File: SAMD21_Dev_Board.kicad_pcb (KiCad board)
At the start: 2 copper layers, 55.4 x 87.4 mm, 88 parts, among them J1 SWD, J10 JST_SH_SM06B-SRSS-TB_1x06-1MP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, J11 JST_SH_SM06B-SRSS-TB_1x06-1MP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, J12 JST_SH_SM06B-SRSS-TB_1x06-1MP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, J13 JST_SH_SM06B-SRSS-TB_1x06-1MP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, J14 JST_SH_SM06B-SRSS-TB_1x06-1MP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, J15 JST_SH_SM06B-SRSS-TB_1x06-1MP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, J16 JST_SH_SM06B-SRSS-TB_1x06-1MP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, J17 Status LED, J2 USB_C_Receptacle_USB2.0_16P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

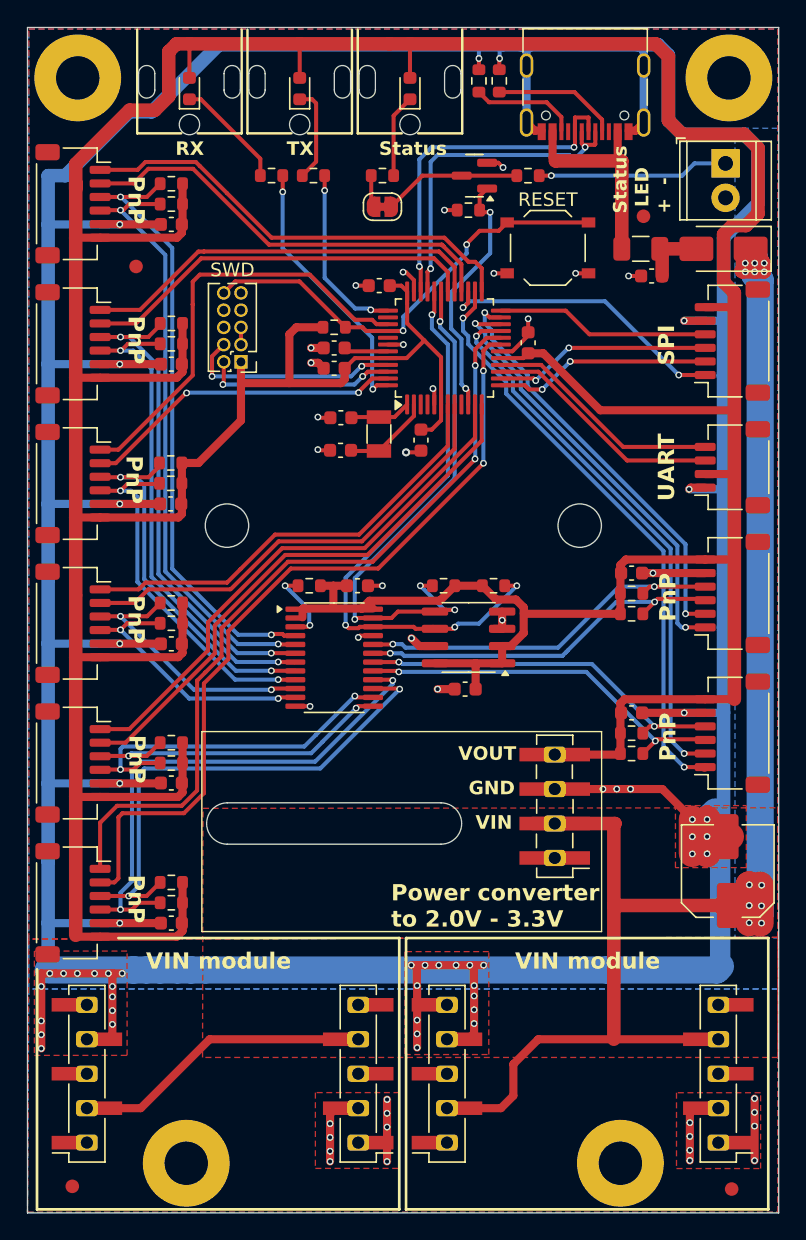
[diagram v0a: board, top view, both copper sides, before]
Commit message: Back to cables with GND pin1, VCC pin2
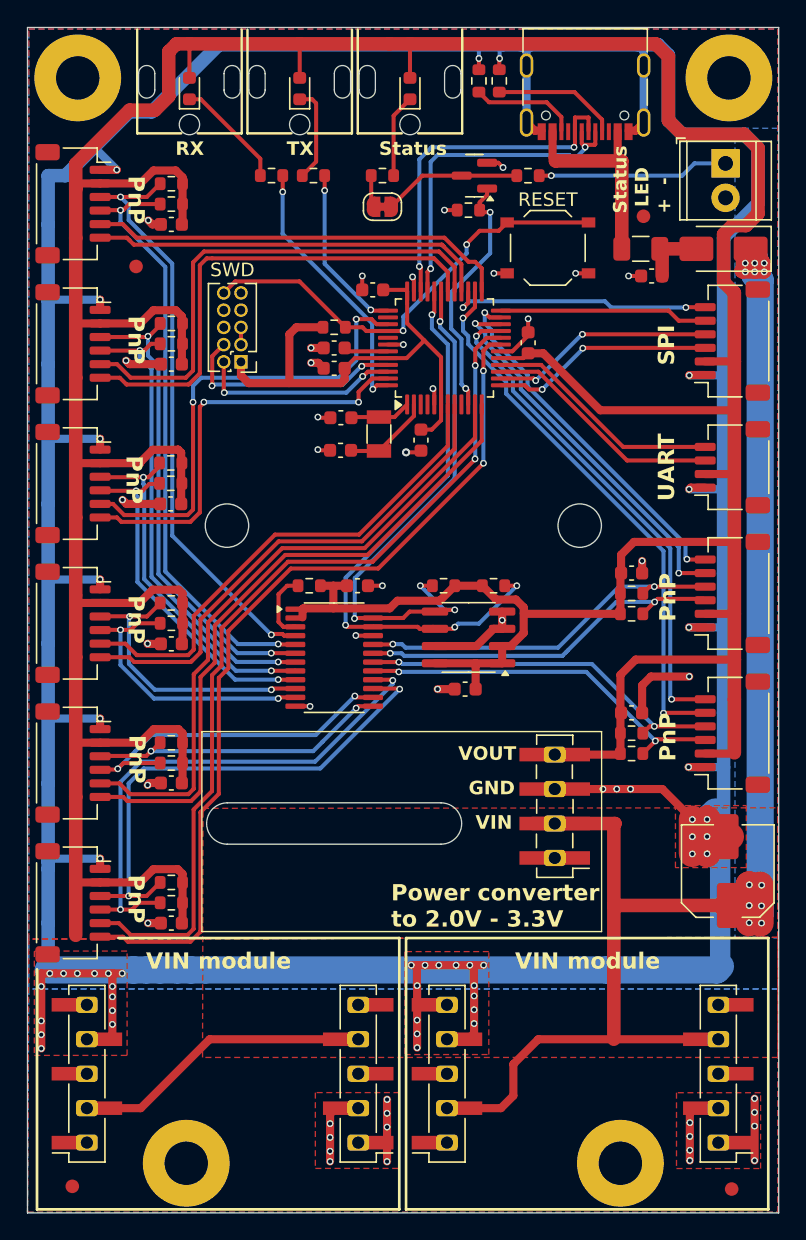
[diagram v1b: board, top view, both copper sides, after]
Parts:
- moved C16 0.57 mm to (107.7, 69.1)
- turned C5 to 180 degrees
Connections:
- C5 pad 1: GND -> VCC
- C5 pad 2: VCC -> GND
- J10 pad 1: D13 -> GND
- J10 pad 2: D22 -> VCC
- J10 pad 5: GND -> D13
- J10 pad 6: VCC -> D22
- J11 pad 1: D24 -> GND
- J11 pad 2: D23 -> VCC
- J11 pad 5: GND -> D24
- J11 pad 6: VCC -> D23
- J12 pad 1: D8 -> GND
- J12 pad 2: D9 -> VCC
- J12 pad 5: GND -> D8
- J12 pad 6: VCC -> D9
- J13 pad 1: D11 -> GND
- J13 pad 2: D12 -> VCC
- J13 pad 5: GND -> D11
- J13 pad 6: VCC -> D12
- J14 pad 1: D6 -> GND
- J14 pad 2: D7 -> VCC
- J14 pad 5: GND -> D6
- J14 pad 6: VCC -> D7
- J15 pad 1: D26 -> GND
- J15 pad 2: A5 -> VCC
- J15 pad 5: GND -> D26
- J15 pad 6: VCC -> A5
- J16 pad 1: A1 -> GND
- J16 pad 2: A2 -> VCC
- J16 pad 5: GND -> A1
- J16 pad 6: VCC -> A2
- J8 pad 1: D10/SPI_SS -> GND
- J8 pad 2: SPI_MOSI -> VCC
- J8 pad 3: SPI_MISO -> SPI_MOSI
- J8 pad 4: SPI_SCK -> SPI_MISO
- J8 pad 5: GND -> SPI_SCK
- J8 pad 6: VCC -> D10/SPI_SS
- J9 pad 1: D38 -> GND
- J9 pad 2: D2 -> VCC
- J9 pad 5: GND -> D38
- J9 pad 6: VCC -> D2
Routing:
- net GND: track 447.4 -> 427.9 mm, vias 86 -> 93
- net D8: track 40.2 -> 47.9 mm
- net D9: track 41.2 -> 48.5 mm
- net D6: track 30.2 -> 37.3 mm
- net A5: track 23.9 -> 30.8 mm
- net D7: track 29.5 -> 36.2 mm
- net D24: track 58.4 -> 64.7 mm
- net VCC: track 381.0 -> 387.0 mm
- net D23: track 59.4 -> 64.6 mm
- net D2: track 31.1 -> 27.0 mm
- net D38: track 32.4 -> 28.5 mm
- net A1: track 33.1 -> 36.9 mm
- net D22: track 40.6 -> 37.2 mm
- net A2: track 34.0 -> 37.5 mm
- net D13: track 43.8 -> 40.7 mm
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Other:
- board text added: "GND VCC SDA SCL INT1 INT2"
- board text added: "SS SCK MISO MOSI VCC GND"
- board text removed: "INT2 INT1 SDA SCL GND VCC"
- board text removed: "VCC GND SCK MISO MOSI SS"

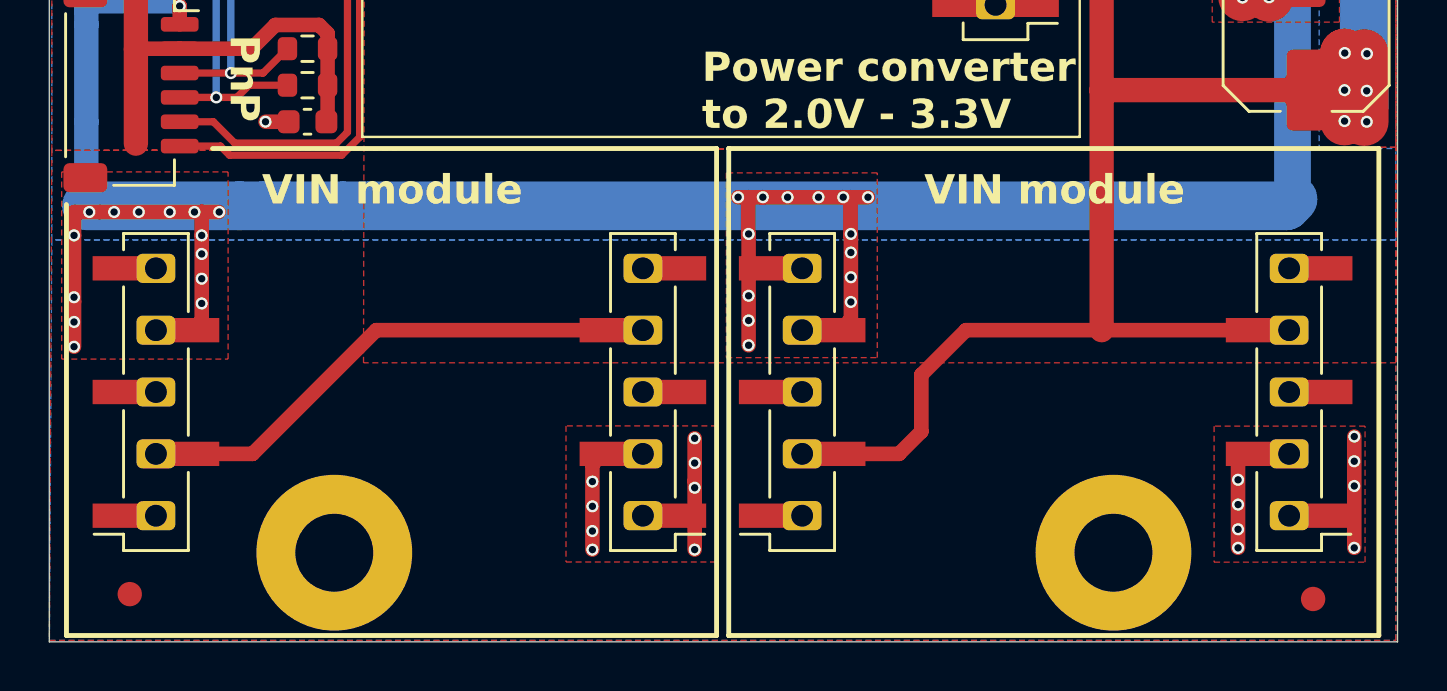
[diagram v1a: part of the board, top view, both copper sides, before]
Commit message: Moved the power modules location to have 1mm more spacing between them
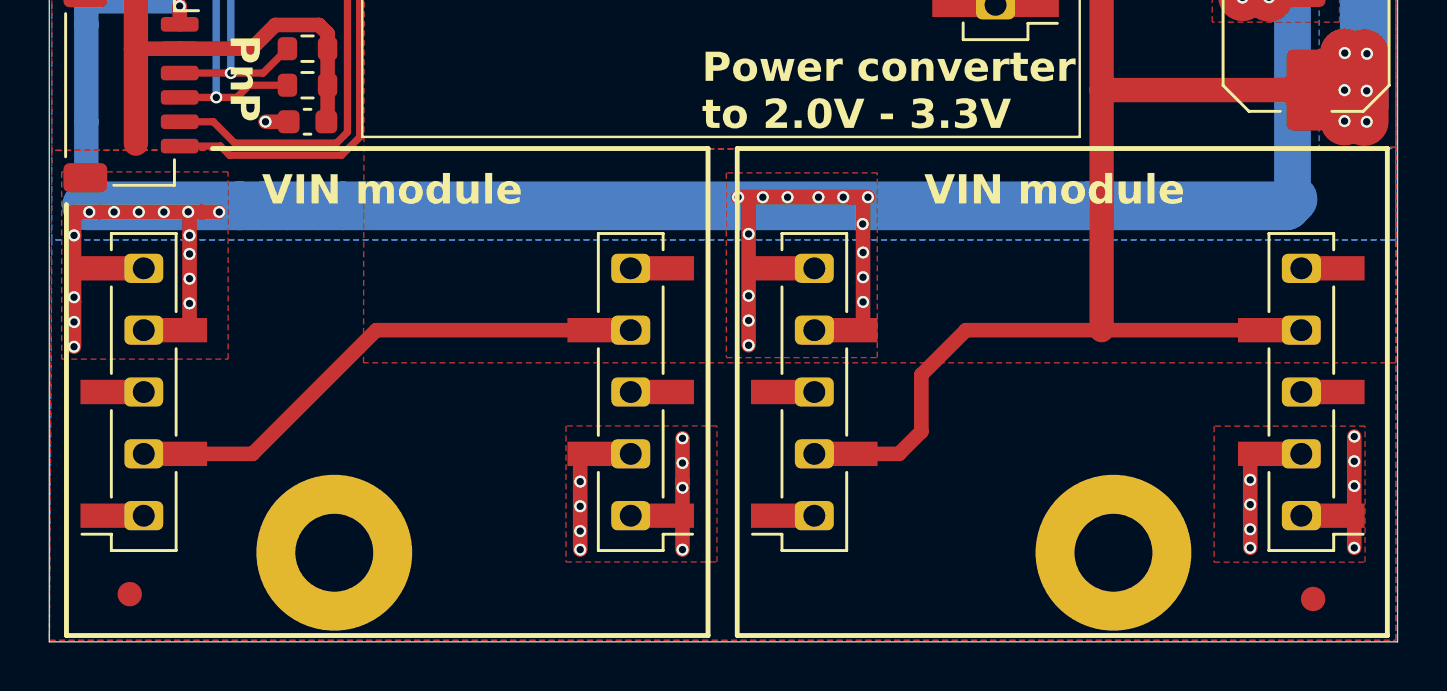
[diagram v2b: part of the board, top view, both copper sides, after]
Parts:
- moved J20 0.50 mm to (86.2, 126.9)
- moved J4 0.50 mm to (106.2, 126.9)
- moved J5 0.50 mm to (113.7, 126.9)
- moved J6 0.50 mm to (133.7, 126.9)
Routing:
- net GND: track 427.9 -> 425.3 mm

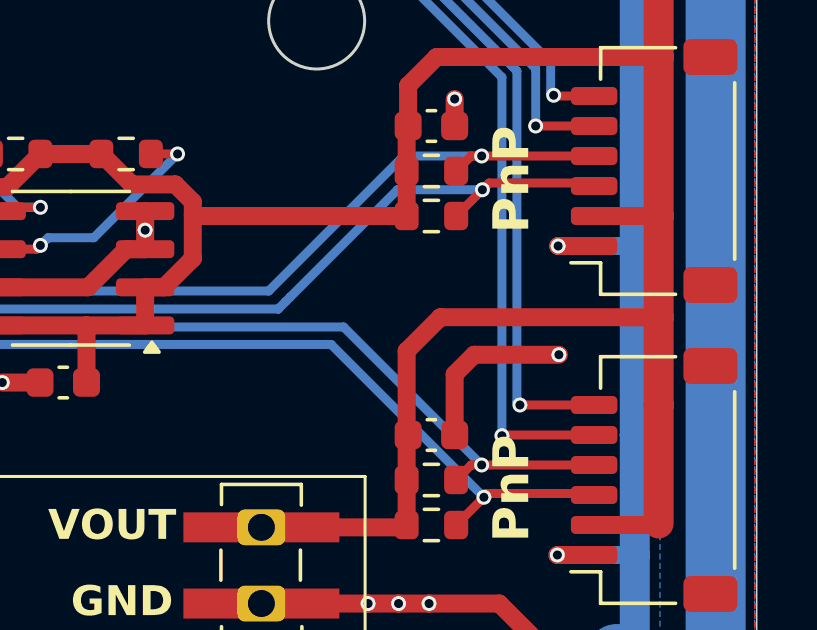
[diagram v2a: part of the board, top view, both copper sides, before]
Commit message: Adding Rev number to the back copper layer
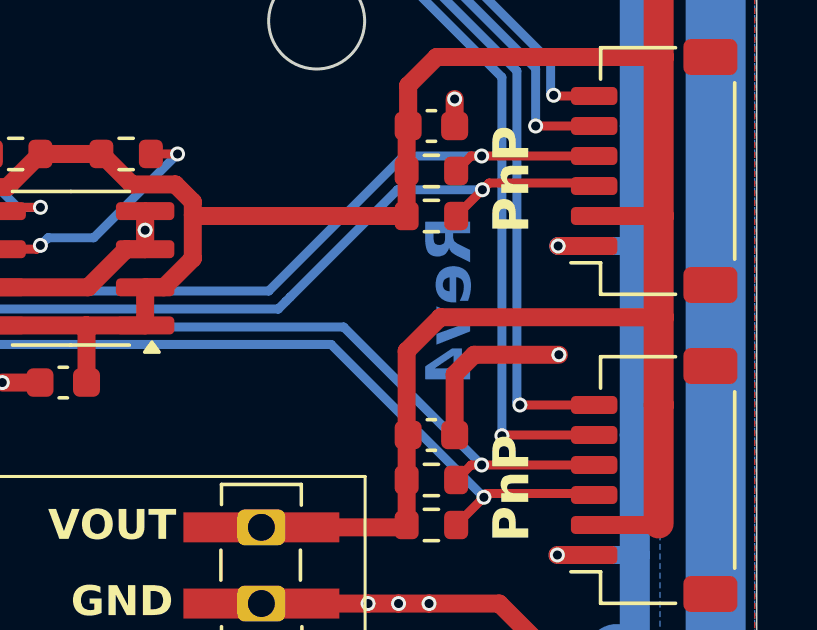
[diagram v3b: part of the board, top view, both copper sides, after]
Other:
- board text added: "Rev4"
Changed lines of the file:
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@@
 		(layer "Edge.Cuts")
+	)
+	(gr_text "Rev4"
+		(at 128.3 93 90)
+		(layer "B.Cu")
+		(effects
+			(font
+				(size 1.5 1.5)
+				(thickness 0.3)
+				(bold yes)
+			)
+			(justify left bottom mirror)
+		)
 	)
 	(gr_text "Rx\nTx\nVCC\nGND\n"

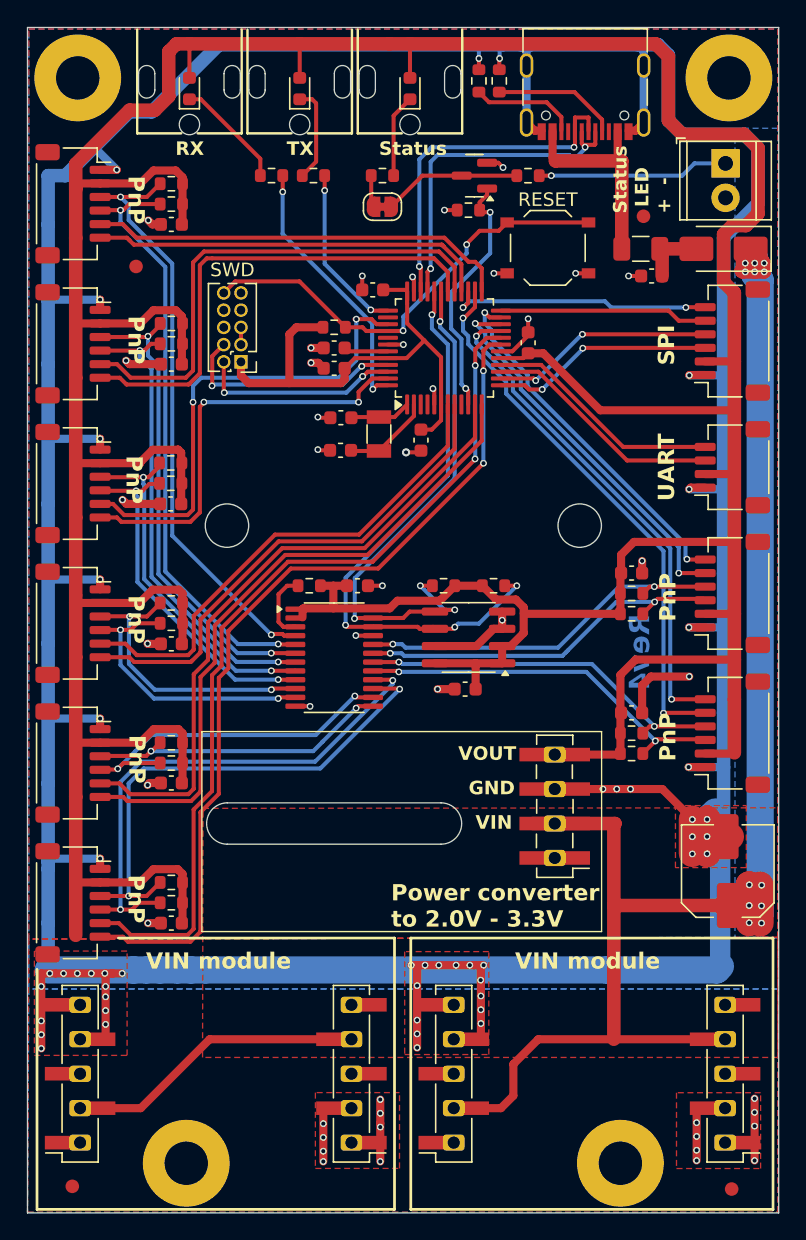
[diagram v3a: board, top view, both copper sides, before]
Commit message: Ground plane return paths improvements
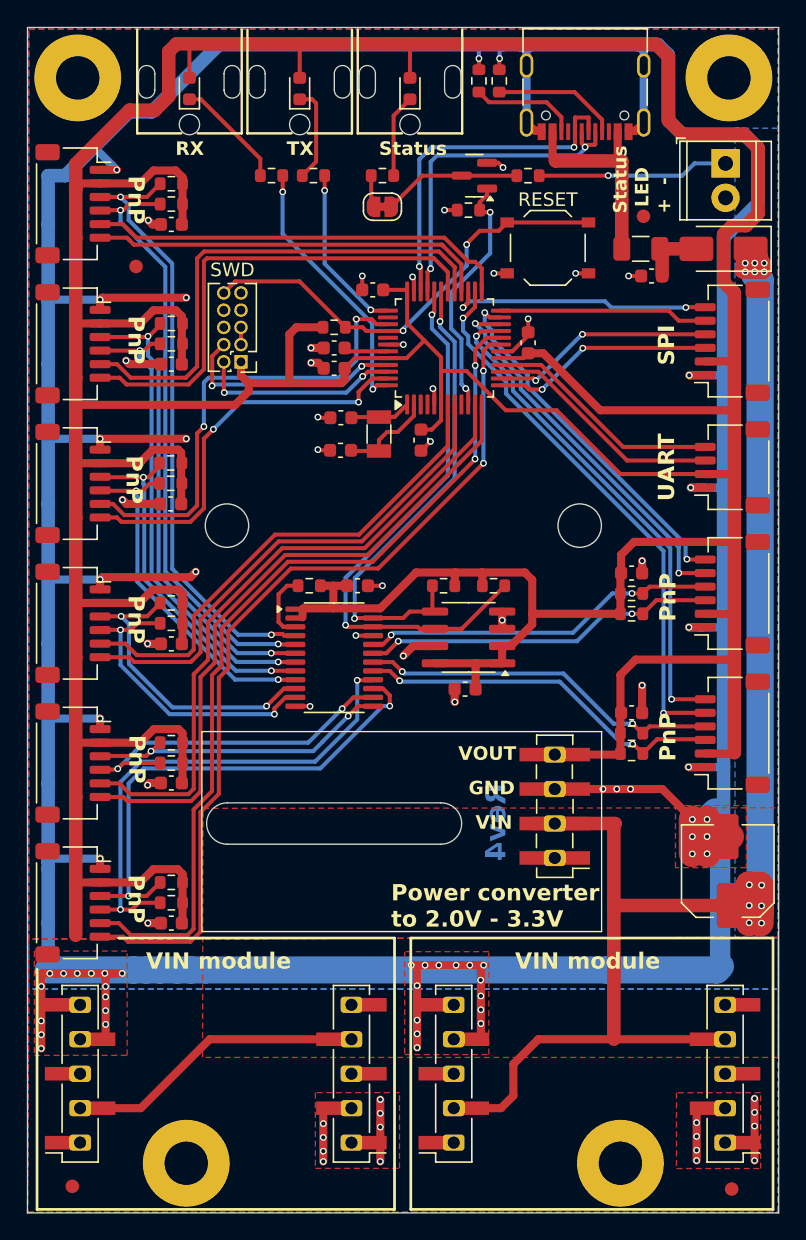
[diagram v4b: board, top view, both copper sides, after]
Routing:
- net VCC: track 387.0 -> 427.6 mm
- net GND: track 425.3 -> 438.0 mm, vias 93 -> 97
- net I2C_SDA: track 39.5 -> 36.5 mm, vias 4 -> 2
- net I2C_SCL: track 43.5 -> 41.8 mm, vias 4 -> 2
- net SDA7: track 27.2 -> 25.6 mm
- net A5: track 30.8 -> 29.3 mm
- net SDA0: track 43.4 -> 44.8 mm
- net SCL5: track 38.7 -> 37.3 mm
- net SDA3: track 21.4 -> 22.6 mm
- net SCL3: track 21.0 -> 22.2 mm
- net SDA5: track 37.9 -> 36.9 mm
- net SCL7: track 27.0 -> 26.0 mm
- net SCL6: track 27.0 -> 26.3 mm
